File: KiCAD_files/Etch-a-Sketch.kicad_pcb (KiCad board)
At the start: 2 copper layers, 98 x 85.5 mm, 45 parts, among them J1 Debug Connector, J2 Display / Mounting Socket, J3 Display Mounting Socket, P1 282837-2, U1 STM32L433CCTx, U2 W25Q64JV, U3 ICM-42688-P, U6 Adafruit 377 Rotary Encoder, U7 Adafruit 377 Rotary Encoder

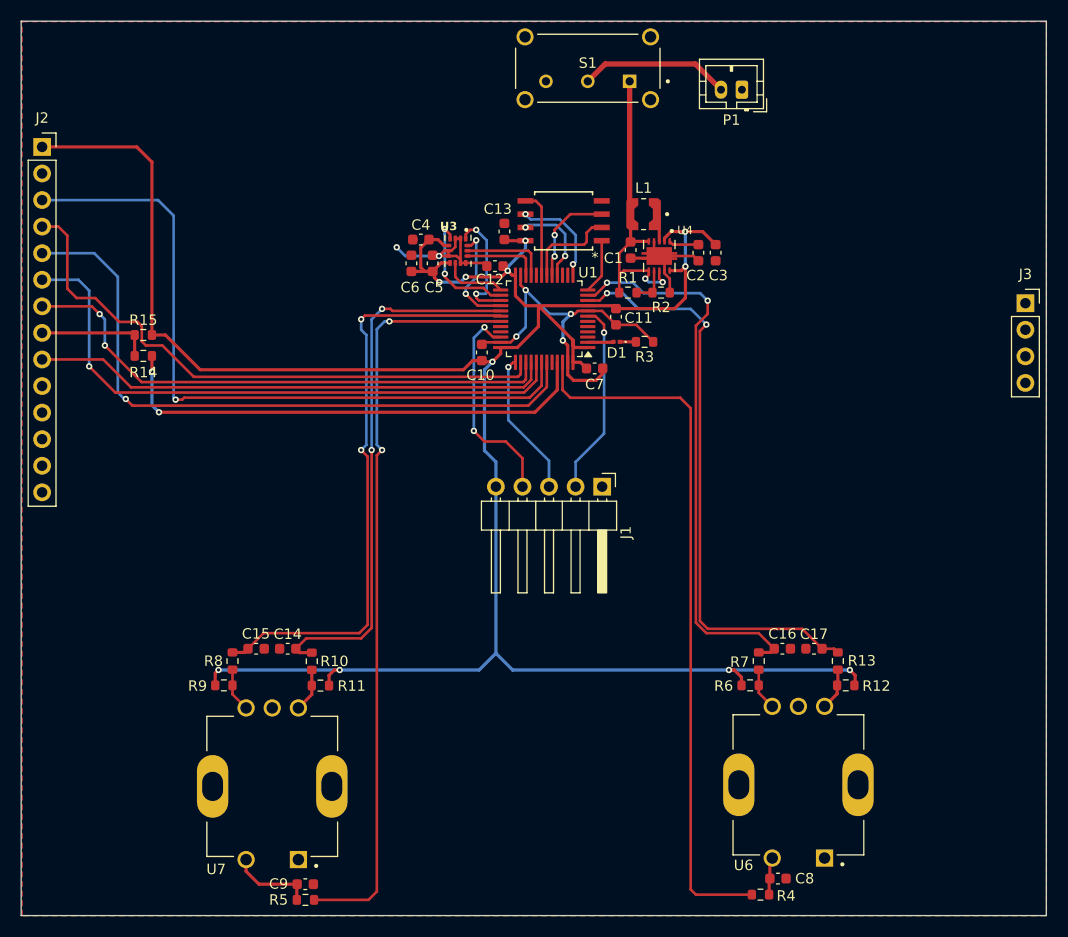
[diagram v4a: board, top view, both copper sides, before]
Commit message: Initial Rev1 Changes, including
Mounting holes
Switch to choose backlight reference to replace jumper resistors
Pull ups/downs for NRST and BOOT0
Move the debug connector location
Relabel passive components
Add jumper resistors to remove power from ICs
Add diode to prevent reverse powering
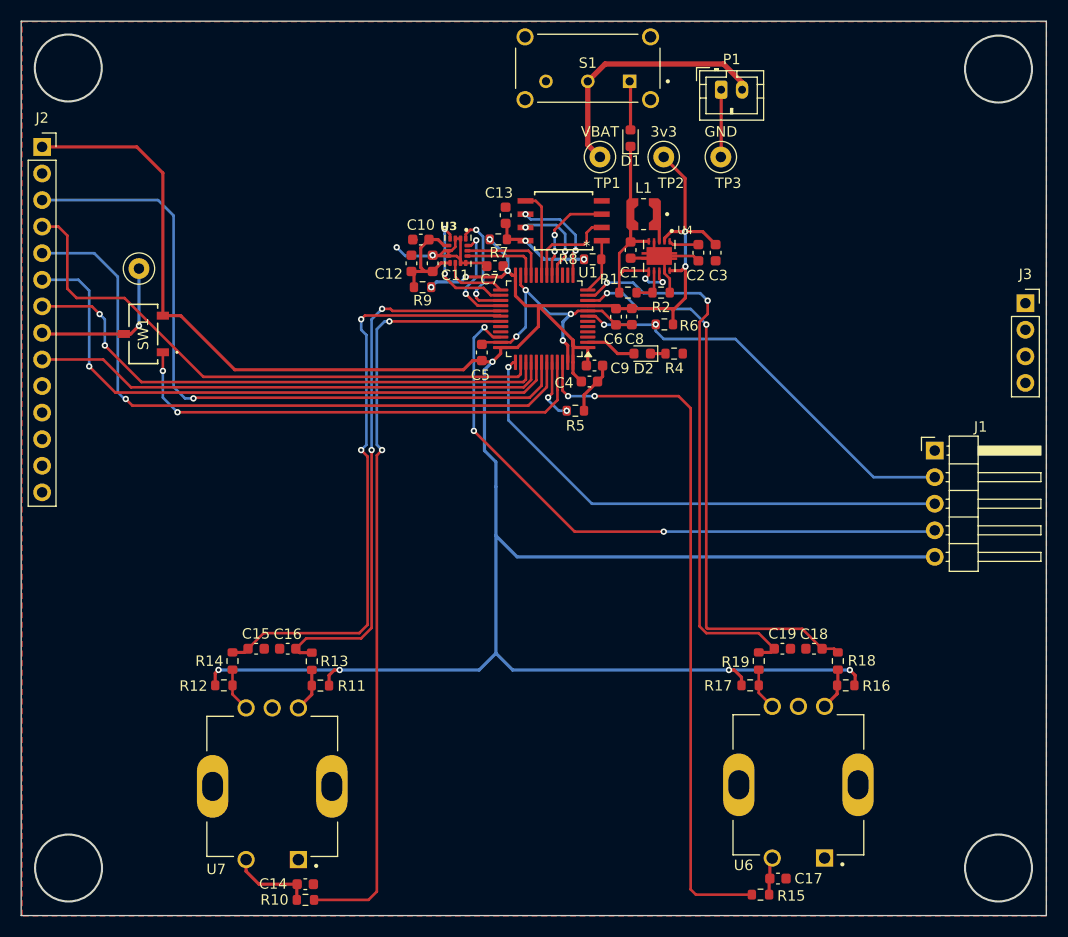
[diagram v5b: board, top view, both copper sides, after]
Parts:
- removed the R14 at (116.1, 84.0)
- removed the R15 at (116.1, 82.0)
- added C8: 1uF, Capacitor_SMD:C_0603_1608Metric, F.Cu at (162.8, 80.3)
- added C9: 4.7uF, Capacitor_SMD:C_0603_1608Metric, F.Cu at (159.2, 85.0)
- added D1: D_Schottky, Diode_SMD:D_0603_1608Metric, F.Cu at (162.7, 63.2)
- added R5: 10K, Resistor_SMD:R_0603_1608Metric, F.Cu at (157.4, 89.3)
- added R6: 10K, Resistor_SMD:R_0603_1608Metric, F.Cu at (165.9, 81.0)
- added R7: 0, Resistor_SMD:R_0603_1608Metric, F.Cu at (150.1, 72.9)
- added R8: 10k, Resistor_SMD:R_0603_1608Metric, F.Cu at (159.1, 74.8)
- added R9: 0, Resistor_SMD:R_0603_1608Metric, F.Cu at (142.8, 77.5)
- added SW1: Backlight Select, Switch_footprint:CJS-1200B_NDC, F.Cu at (116.1, 81.9)
- added TP1: VBAT, TestPoint:TestPoint_Loop_D1.80mm_Drill1.0mm_Beaded, F.Cu at (159.8, 65.0)
- added TP2: 3v3, TestPoint:TestPoint_Loop_D1.80mm_Drill1.0mm_Beaded, F.Cu at (165.9, 65.0)
- added TP3: GND, TestPoint:TestPoint_Loop_D1.80mm_Drill1.0mm_Beaded, F.Cu at (171.3, 65.0)
- added TP4: LED, TestPoint:TestPoint_Loop_D1.80mm_Drill1.0mm_Beaded, F.Cu at (115.7, 75.7)
- C1: value 4.7uF -> 10uF
- C2: value 0.12uF -> 0.1uF
- C3: value 12uF -> 10uF
- D2: renamed from D1; footprint LED_SMD:LED_0201_0603Metric -> LED_SMD:LED_0603_1608Metric
- moved J1 32.0 mm to (191.8, 93.1), turned to 0 degrees
- moved R4 3.04 mm to (166.9, 83.8)
- moved D2 2.69 mm to (163.8, 83.8)
- moved P1 1.98 mm to (171.4, 58.6), turned to 0 degrees
- moved C13 1.55 mm to (150.7, 70.6)
- moved C4 1.34 mm to (158.8, 86.5)
- renumbered C4 to C10, C5 to C11, C6 to C12, C9 to C14, C14 to C16, C8 to C17, C17 to C18, C16 to C19, C7 to C4, C10 to C5, C11 to C6, C12 to C7, R5 to R10, R9 to R12, R10 to R13, R8 to R14, R4 to R15, R12 to R16, R6 to R17, R13 to R18, R7 to R19, R3 to R4
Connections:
- net Net-(P1-Pad2) renamed /VBAT
- C1 pad 1: Net-(U4-EN) -> Net-(D1-K)
- C10 pad 1: +3V3 -> /ICM_VDD
- C11 pad 1: +3V3 -> /ICM_VDD
- C12 pad 1: +3V3 -> /ICM_VDD
- C13 pad 1: +3V3 -> Net-(U2-3V3)
- J2 pad 8: Net-(J2-Pin_8) -> /LED
- L1 pad 2: Net-(U4-EN) -> Net-(D1-K)
- R1 pad 1: Net-(U4-EN) -> Net-(D1-K)
- S1 pad 1: Net-(U4-EN) -> Net-(D1-A)
- U1 pad 44: unconnected-(U1-PH3-Pad44) -> /BOOT0
- U1 pad 45: /LED -> /LED_PWM
- U2 pad 8: +3V3 -> Net-(U2-3V3)
- U3 pad 5: +3V3 -> /ICM_VDD
- U3 pad 8: +3V3 -> /ICM_VDD
- U4 pad 5: Net-(U4-EN) -> Net-(D1-K)
- U4 pad 6: Net-(U4-EN) -> Net-(D1-K)
- U4 pad 8: Net-(U4-EN) -> Net-(D1-K)
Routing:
- net /LED_PWM: track 0.00 -> 46.7 mm, vias 0 -> 2
- net +3V3: track 237.7 -> 278.5 mm
- net /DEBUG_DIO: track 20.8 -> 60.4 mm, vias 2 -> 3
- net /DEBUG_CLK: track 13.9 -> 50.0 mm
- net /LED: track 47.3 -> 15.1 mm, vias 2 -> 1
- net Net-(U4-EN): track 29.8 -> 0.00 mm, vias 2 -> 0
- net Net-(D1-K): track 0.00 -> 23.6 mm, vias 0 -> 2
- net /NRST: track 18.5 -> 39.9 mm, vias 1 -> 2
- net /ICM_VDD: track 0.00 -> 12.3 mm
- net Net-(J2-Pin_8): track 10.9 -> 0.00 mm
- net /VBAT: track 14.4 -> 24.6 mm
- net Net-(U2-3V3): track 0.00 -> 9.86 mm, vias 0 -> 2
- net /BOOT0: track 0.00 -> 5.97 mm, vias 0 -> 2
- net Net-(D1-A): track 0.00 -> 4.68 mm
- net GND: track 63.8 -> 67.3 mm
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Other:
- outline, holes or cut-outs redrawn
